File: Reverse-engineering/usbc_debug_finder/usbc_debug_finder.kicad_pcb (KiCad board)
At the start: 2 copper layers, 27 x 11 mm, 22 parts, among them J1 USB_C_Plug

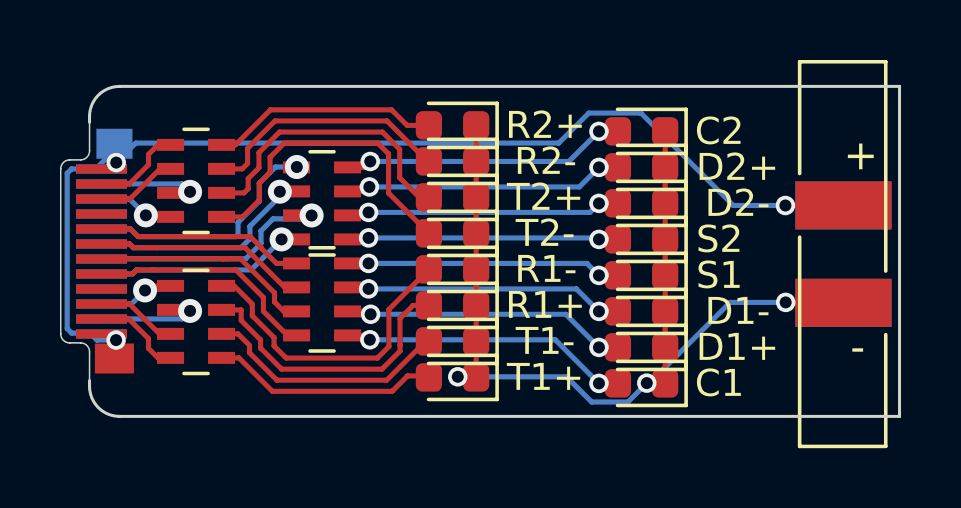
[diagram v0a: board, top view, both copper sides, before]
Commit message: usbc_debug_finder: v1 (new, actual to-be-ordered)
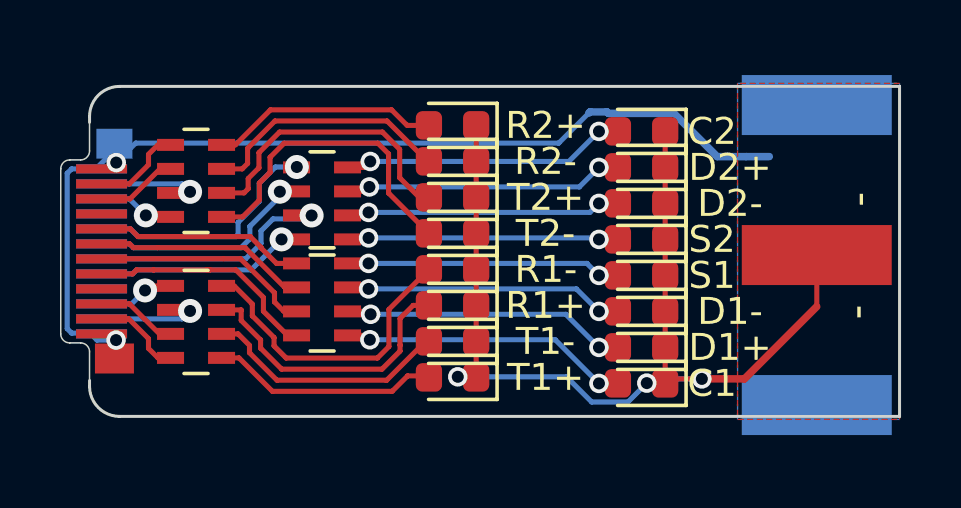
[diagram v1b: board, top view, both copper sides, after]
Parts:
- BT1: footprint Battery:Battery_Panasonic_CR1220-VCN_Vertical_CircularHoles -> usbc_debug_finder:BAT-TH_BS-05-A1BJ001
- moved BT1 2.63 mm to (142.2, 87.1)
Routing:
- net GND: track 41.7 -> 35.8 mm, vias 3 -> 2
- added copper zone on F.Cu, net -3V3
- added copper zone on B.Cu, net GND
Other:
- board text added: "USB2 & SB signals"
- board text added: "trans rights"
